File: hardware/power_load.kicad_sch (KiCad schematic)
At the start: 42 parts, among them J401 Screw_Terminal_3P, J402 Screw_Terminal_3P, Q401 IRF530PBF, U401 TSB611ILT, U402 INA228, U403 LM35-NEB, U404 TSB611ILT

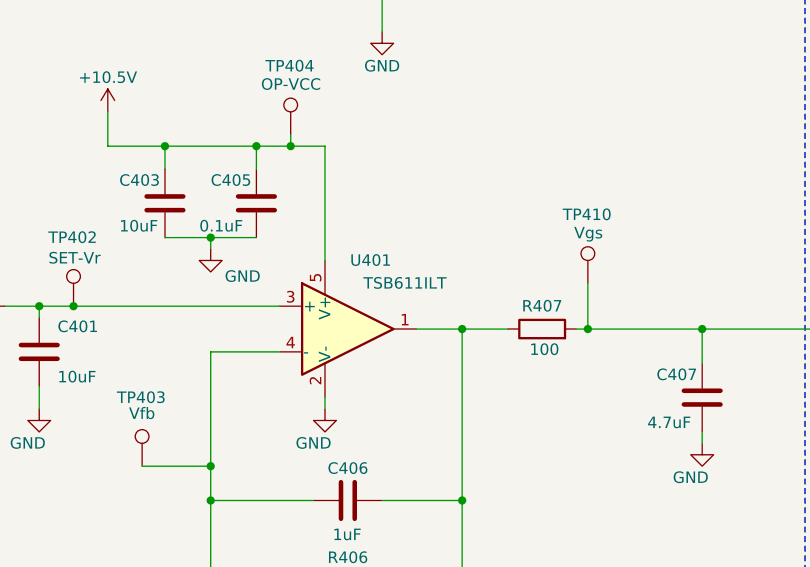
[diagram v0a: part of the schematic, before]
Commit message: Changed OpAMP part no.
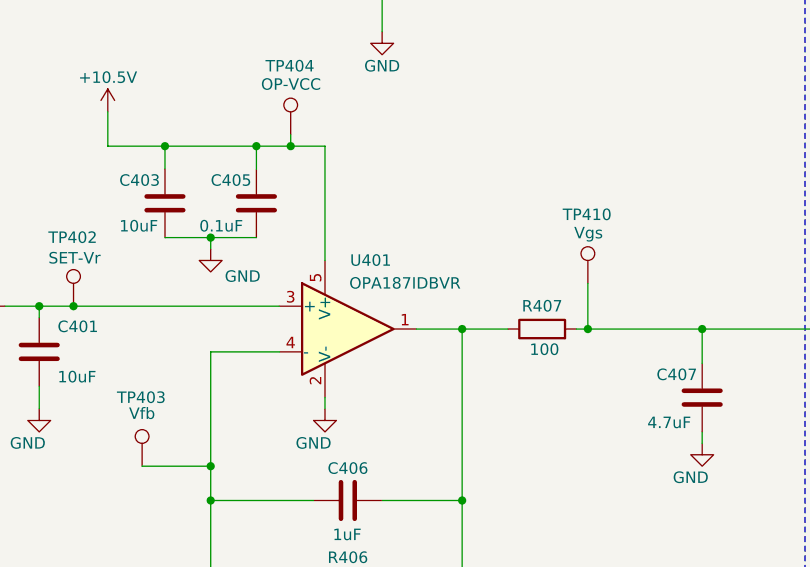
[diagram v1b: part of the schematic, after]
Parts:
- TP-PAD401: digikey (none) -> 2019-RCWCTECT-ND; distributor (none) -> https://www.digikey.jp/en/products/detail/koa-speer-electro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
- U401: value TSB611ILT -> OPA187IDBVR
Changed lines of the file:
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@@
 			)
 		)
-		(property "Value" "TSB611ILT"
+		(property "Value" "OPA187IDBVR"
 			(at 102.87 82.55 0)
 			(effects
@@
 			(at 86.36 157.48 0)
 			(effects
+				(font
+					(size 1.27 1.27)
+				)
+				(hide yes)
+			)
+		)
+		(property "digikey" "2019-RCWCTECT-ND"
+			(at 86.36 157.48 0)
+			(effects
+				(font
+					(size 1.27 1.27)
+				)
+				(hide yes)
+			)
+		)
+		(property "distributor" "https://www.digikey.jp/en/products/detail/koa-speer-electronics-inc/RCWCTE/11476558"
+			(at 86.36 157.48 0)
+			(effects
